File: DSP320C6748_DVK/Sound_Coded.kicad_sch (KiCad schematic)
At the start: 44 parts, among them IC15 TLV320AIC3106IRGZT, J10 SJ-3524-SMT-BE, J11 SJ-3524-SMT-BE, J9 SJ-3524-SMT-BE, Y5 ASFL1-24.576MHZ-EC-T

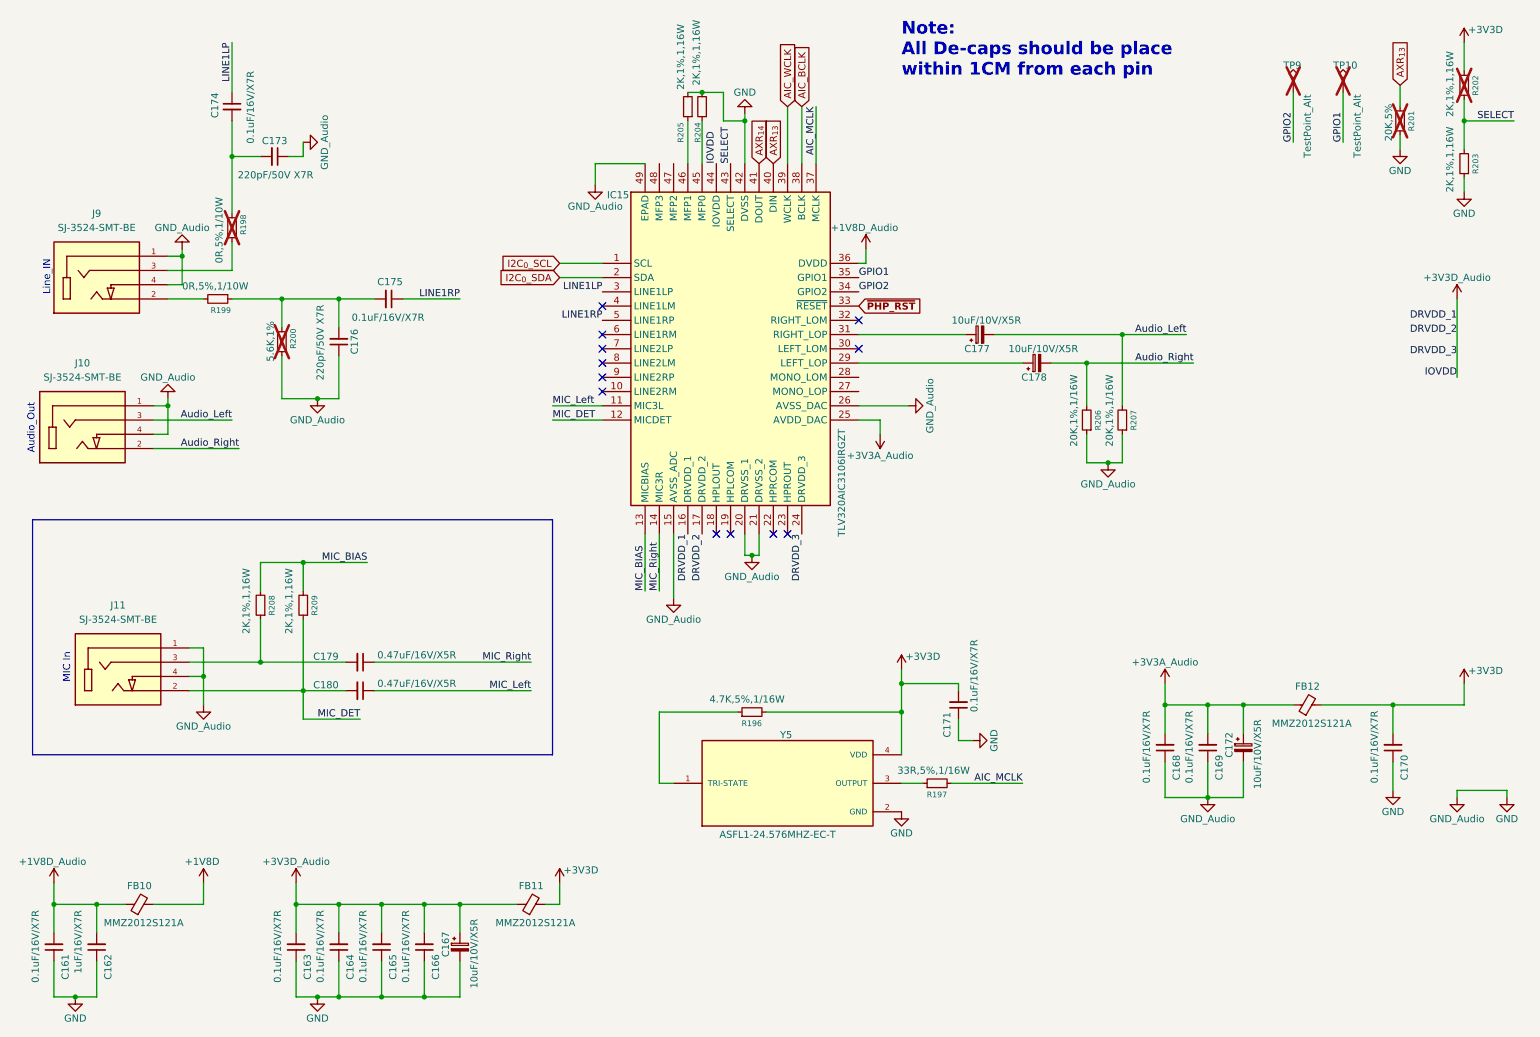
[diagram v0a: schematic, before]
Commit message: LAN Schematic Added
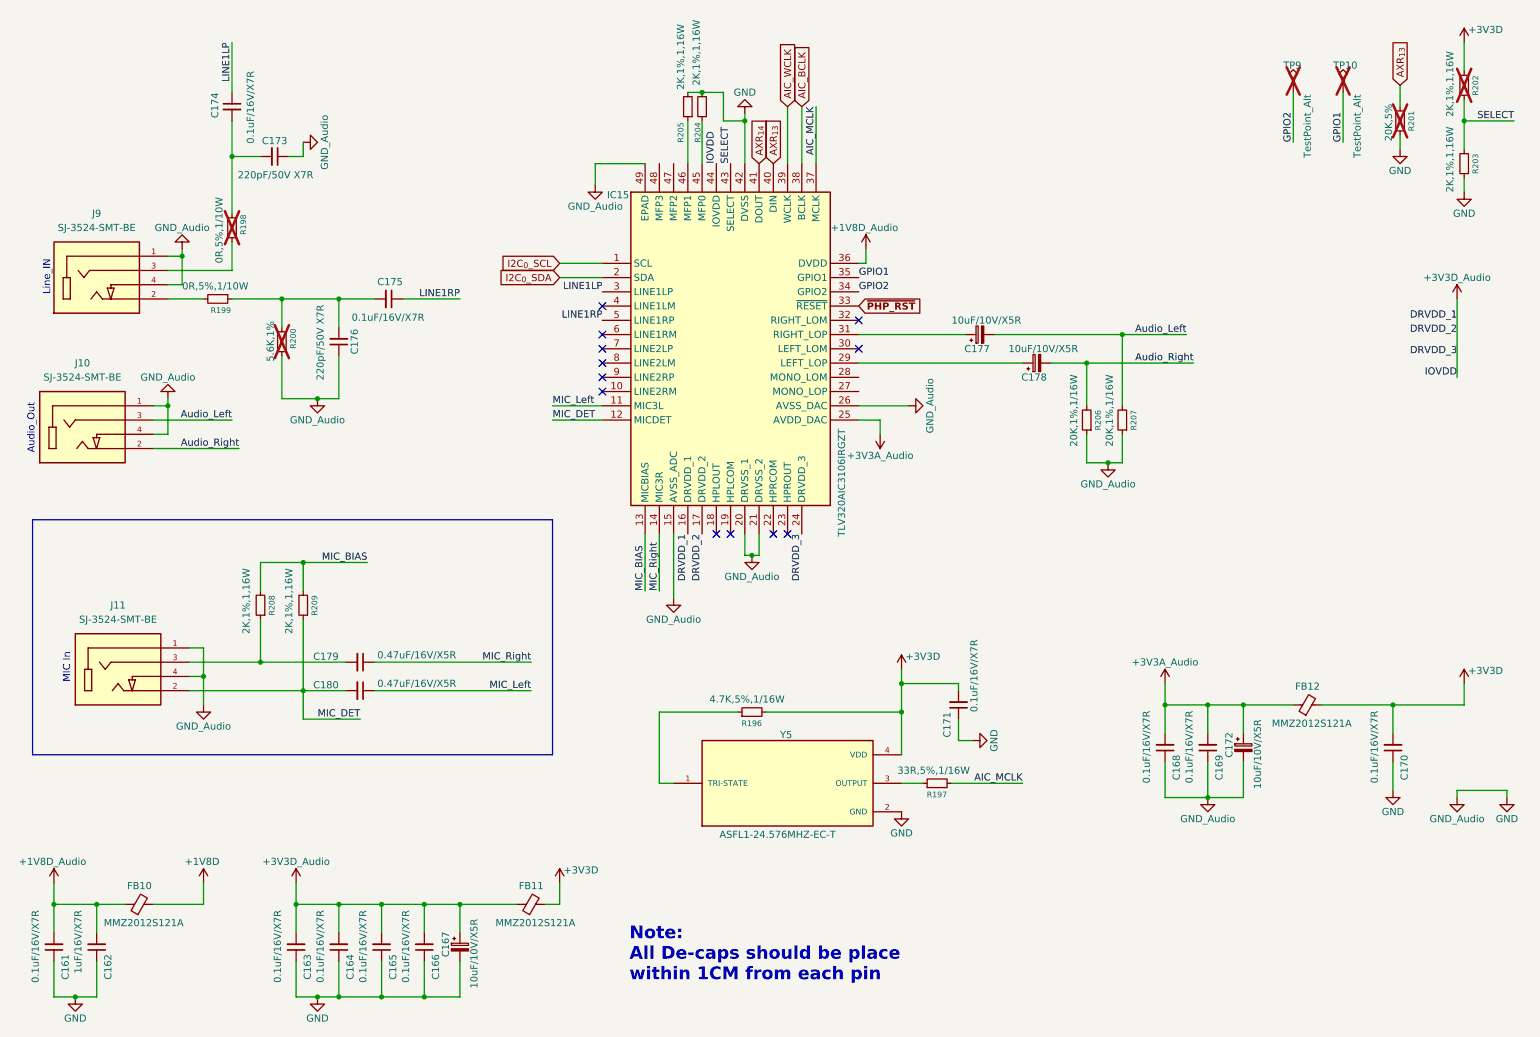
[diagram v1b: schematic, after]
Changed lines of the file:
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@@
 	(text "Note:\nAll De-caps should be place\nwithin 1CM from each pin"
 		(exclude_from_sim no)
-		(at 171.45 22.86 0)
+		(at 122.936 184.15 0)
 		(effects
 			(font

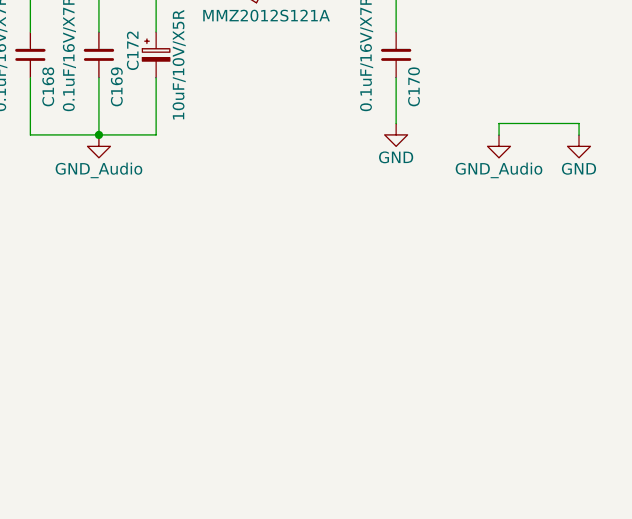
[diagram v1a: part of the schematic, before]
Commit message: Connectors and mislleneous components added
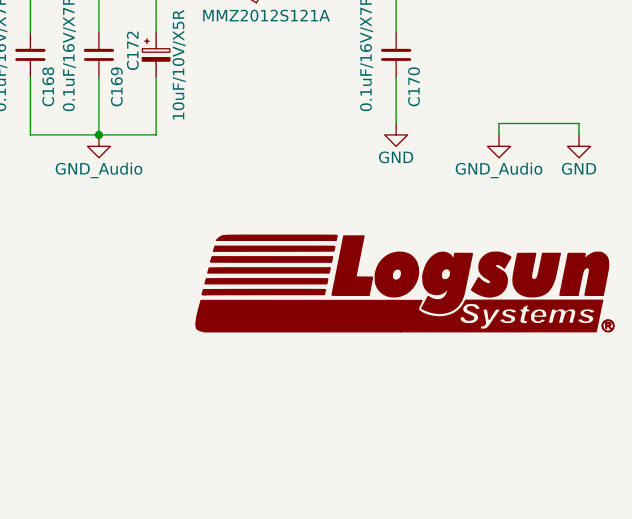
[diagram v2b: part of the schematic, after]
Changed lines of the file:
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@@
+	)
+	(symbol
+		(lib_id "Logsun_Logo:LOGO")
+		(at 260.35 172.72 0)
+		(unit 1)
+		(body_style 1)
+		(exclude_from_sim no)
+		(in_bom yes)
+		(on_board yes)
+		(in_pos_files yes)
+		(dnp no)
+		(fields_autoplaced yes)
+		(property "Reference" "#G12"
+			(at 260.35 166.755 0)
+			(hide yes)
+			(show_name no)
+			(do_not_autoplace no)
+			(effects
+				(font
+					(size 1.27 1.27)
+				)
+			)
+		)
+		(property "Value" "LOGO"
+			(at 260.35 178.685 0)
+			(hide yes)
+			(show_name no)
+			(do_not_autoplace no)
+			(effects
+				(font
+					(size 1.27 1.27)
+				)
+			)
+		)
+		(property "Footprint" ""
+			(at 260.35 172.72 0)
+			(hide yes)
+			(show_name no)
+			(do_not_autoplace no)
+			(effects
+				(font
+					(size 1.27 1.27)
+				)
+			)
+		)
+		(property "Datasheet" ""
+			(at 260.35 172.72 0)
+			(hide yes)
+			(show_name no)
+			(do_not_autoplace no)
+			(effects
+				(font
+					(size 1.27 1.27)
+				)
+			)
+		)
+		(property "Description" ""
+			(at 260.35 172.72 0)
+			(hide yes)
+			(show_name no)
+			(do_not_autoplace no)
+			(effects
+				(font
+					(size 1.27 1.27)
+				)
+			)
+		)
+		(instances
+			(project "DSP320C6748_DVK"
+				(path "/3a70ffc0-9fe7-4a5b-b3c2-23140355df82/66708163-42aa-4cc7-a1d8-21fa6d1e60c9"
+					(reference "#G12")
+					(unit 1)
+				)
+			)
+		)
 	)
 	(symbol

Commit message: Whole Schematic Reannotation Done
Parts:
- renumbered C161 to C171, C162 to C172, C174 to C173, C173 to C174, C163 to C175, C164 to C177, C179 to C178, C180 to C179, C165 to C180, C175 to C181, C166 to C182, C167 to C183, C171 to C184, C177 to C185, C178 to C186, C168 to C187, C169 to C188, C172 to C189, C170 to C190, FB10 to FB11, FB11 to FB12, FB12 to FB13, IC15 to IC16, J9 to J10, J10 to J9, R199 to R170, R198 to R171, R208 to R172, R200 to R173, R209 to R174, R205 to R175, R204 to R176, R196 to R177, R197 to R178, R206 to R179, R207 to R180, R201 to R181, R202 to R182, R203 to R183, TP9 to TP16, TP10 to TP17

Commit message: Schematic Corrections-II Done
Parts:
- added R266: 5.6K,1%, symbol Device:R_Small
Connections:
- net Audio_Left: now also C186.2, R179.2; no longer C185.2, R180.2
- net Audio_Right: now also C185.2, R180.2; no longer C186.2, R179.2
- net GND: now also R266.2
- net at C173.2, C174.2, R171.1: now also R266.1
- no-connect marks 12 -> 16
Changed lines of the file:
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@@
+	)
+	(junction
+		(at 52.07 50.8)
+		(diameter 0)
+		(color 0 0 0 0)
 	)
 	(junction
@@
 	(junction
 		(at 171.45 140.97)
+		(diameter 0)
+		(color 0 0 0 0)
+	)
+	(junction
+		(at 64.77 41.91)
 		(diameter 0)
 		(color 0 0 0 0)
@@
 	)
 	(no_connect
+		(at 163.83 83.82)
+	)
+	(no_connect
 		(at 118.11 78.74)
+	)
+	(no_connect
+		(at 163.83 81.28)
 	)
 	(no_connect
@@
 	)
 	(no_connect
+		(at 130.81 43.18)
+	)
+	(no_connect
 		(at 140.97 109.22)
 	)
@@
 	)
 	(no_connect
+		(at 128.27 43.18)
+	)
+	(no_connect
 		(at 163.83 76.2)
 	)
@@
 	(wire
 		(pts
+			(xy 52.07 50.8) (xy 58.42 50.8)
+		)
+		(stroke
+			(width 0)
+			(type default)
+		)
+	)
+	(wire
+		(pts
 			(xy 130.81 153.67) (xy 128.27 153.67)
 		)
@@
 	(wire
 		(pts
+			(xy 52.07 50.8) (xy 52.07 41.91)
+		)
+		(stroke
+			(width 0)
+			(type default)
+		)
+	)
+	(wire
+		(pts
 			(xy 38.1 93.98) (xy 53.34 93.98)
 		)
@@
 	(wire
 		(pts
+			(xy 63.5 50.8) (xy 64.77 50.8)
+		)
+		(stroke
+			(width 0)
+			(type default)
+		)
+	)
+	(wire
+		(pts
 			(xy 139.7 35.56) (xy 143.51 35.56)
 		)
@@
 	(wire
 		(pts
-			(xy 52.07 52.07) (xy 52.07 41.91)
+			(xy 64.77 50.8) (xy 64.77 41.91)
+		)
+		(stroke
+			(width 0)
+			(type default)
+		)
+	)
+	(wire
+		(pts
+			(xy 52.07 52.07) (xy 52.07 50.8)
 		)
 		(stroke
@@
 	)
 	(label "Audio_Left"
-		(at 222.25 73.66 180)
+		(at 223.52 78.74 180)
 		(effects
 			(font
@@
 	)
 	(label "Audio_Right"
-		(at 223.52 78.74 180)
+		(at 222.25 73.66 180)
 		(effects
 			(font
@@
 					(unit 1)
 				)
+			)
+		)
+	)
+	(symbol
+		(lib_id "Device:R_Small")
+		(at 60.96 50.8 90)
+		(unit 1)
+		(body_style 1)
+		(exclude_from_sim no)
+		(in_bom yes)
+		(on_board yes)
+		(in_pos_files yes)
+		(dnp yes)
+		(property "Reference" "R266"
+			(at 62.23 48.768 90)
+			(show_name no)
+			(do_not_autoplace no)
+			(effects
+				(font
+					(size 1.016 1.016)
+				)
+				(justify left)
+			)
+		)
+		(property "Value" "5.6K,1%"
+			(at 64.516 52.832 90)
+			(show_name no)
+			(do_not_autoplace no)
+			(effects
+				(font
+					(size 1.27 1.27)
+				)
+				(justify left)
+			)
+		)
+		(property "Footprint" ""
+			(at 60.96 50.8 0)
+			(hide yes)
+			(show_name no)
+			(do_not_autoplace no)
+			(effects
+				(font
+					(size 1.27 1.27)
+				)
+			)
+		)
+		(property "Datasheet" ""
+			(at 60.96 50.8 0)
+			(hide yes)
+			(show_name no)
+			(do_not_autoplace no)
+			(effects
+				(font
+					(size 1.27 1.27)
+				)
+			)
+		)
+		(property "Description" "Resistor, small symbol"
+			(at 60.96 50.8 0)
+			(hide yes)
+			(show_name no)
+			(do_not_autoplace no)
+			(effects
+				(font
+					(size 1.27 1.27)
+				)
+			)
+		)
+		(pin "1"
+		)
+		(pin "2"
+		)
+		(instances
+			(project "DSP320C6748_DVK"
+				(path "/3a70ffc0-9fe7-4a5b-b3c2-23140355df82/66708163-42aa-4cc7-a1d8-21fa6d1e60c9"
+					(reference "R266")
+					(unit 1)
+				)

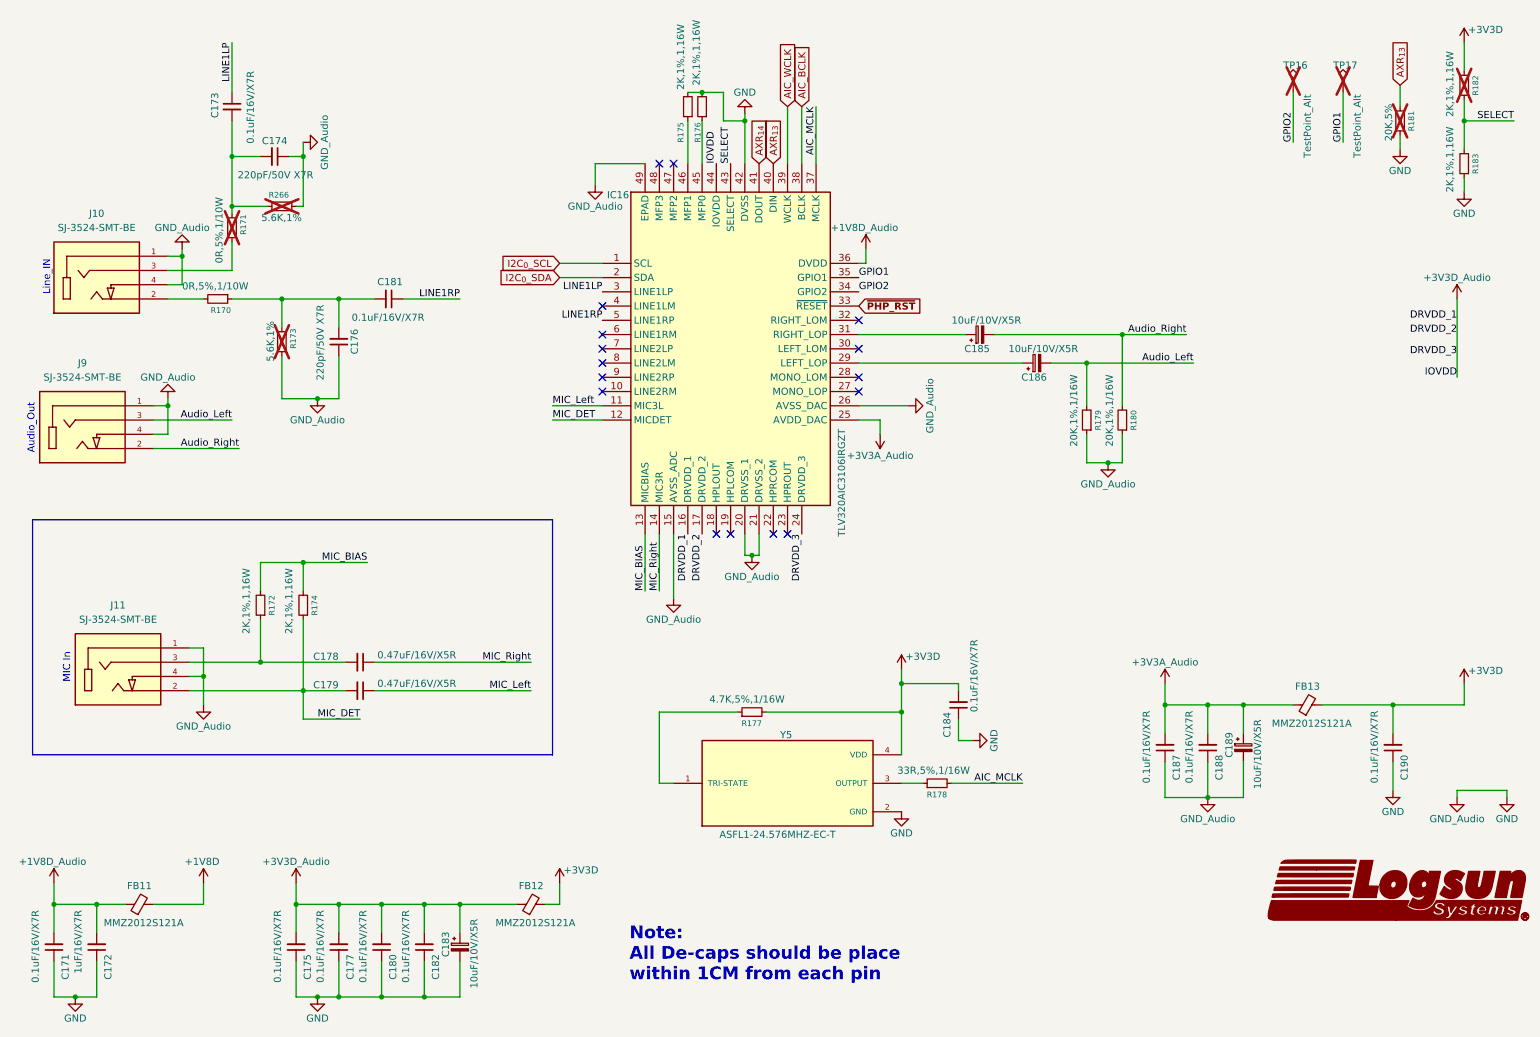
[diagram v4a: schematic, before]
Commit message: DC jack Replaced With Type-C, ADC and RTC section added
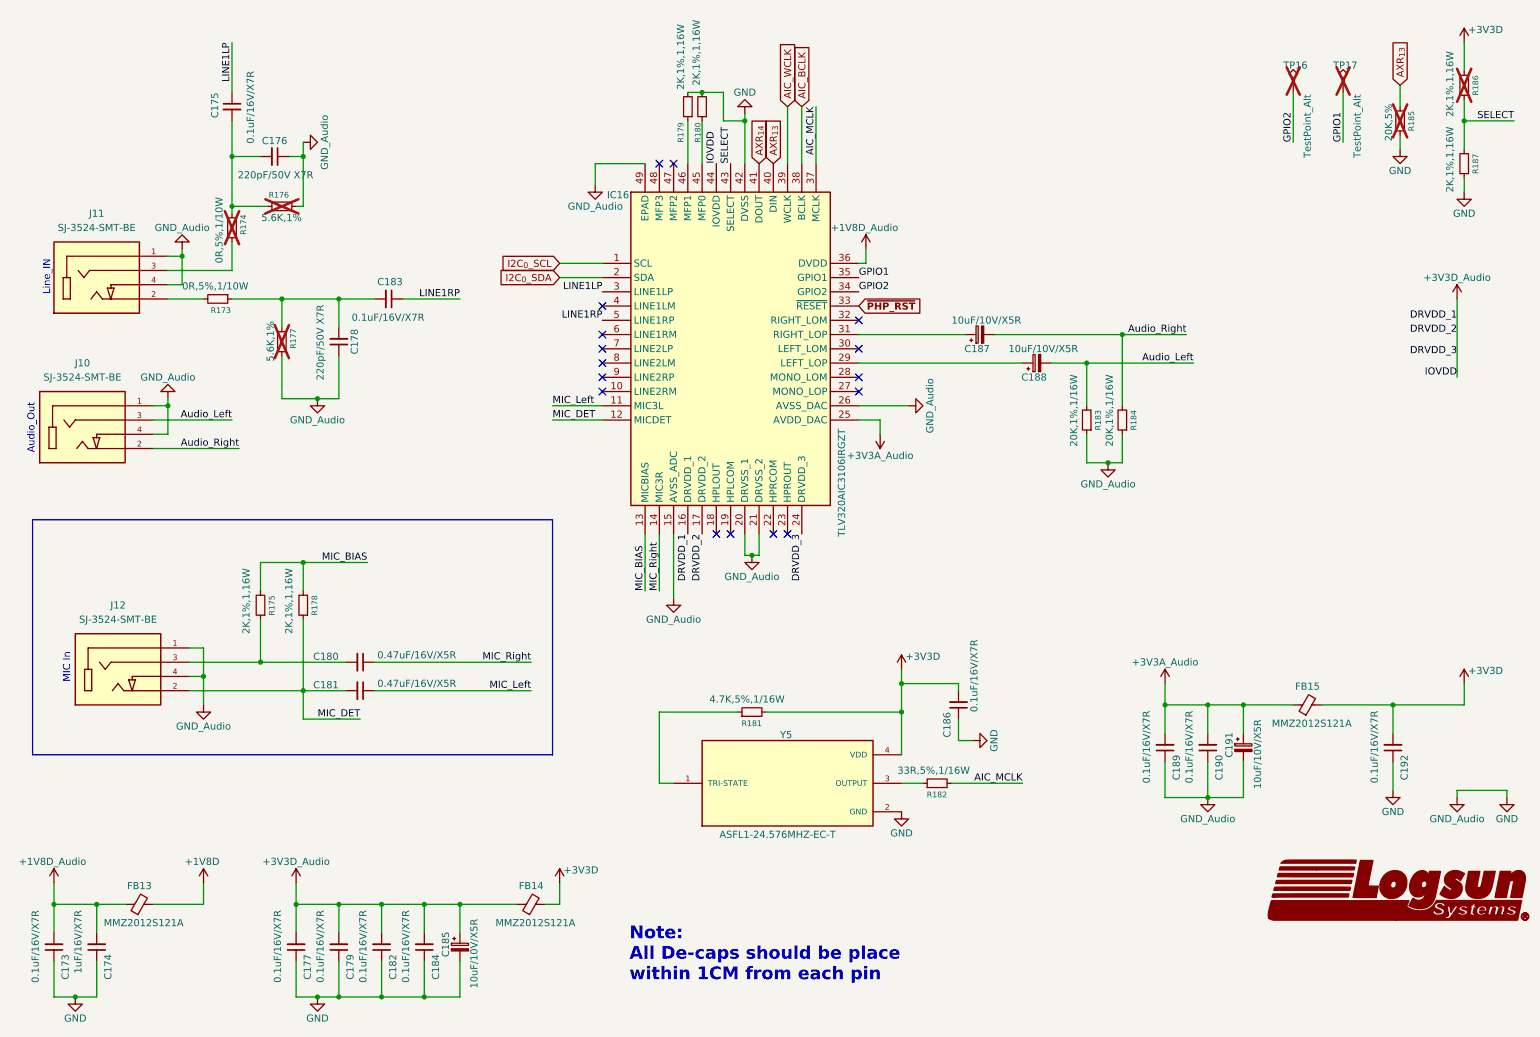
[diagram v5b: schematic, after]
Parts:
- renumbered C171 to C173, C172 to C174, C173 to C175, C174 to C176, C175 to C177, C176 to C178, C177 to C179, C178 to C180, C179 to C181, C180 to C182, C181 to C183, C182 to C184, C183 to C185, C184 to C186, C185 to C187, C186 to C188, C187 to C189, C188 to C190, C189 to C191, C190 to C192, FB11 to FB13, FB12 to FB14, FB13 to FB15, J9 to J10, J10 to J11, J11 to J12, R170 to R173, R171 to R174, R172 to R175, R266 to R176, R173 to R177, R174 to R178, R175 to R179, R176 to R180, R177 to R181, R178 to R182, R179 to R183, R180 to R184, R181 to R185, R182 to R186, R183 to R187
